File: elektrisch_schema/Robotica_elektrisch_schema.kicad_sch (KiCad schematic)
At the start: 13 parts, among them J1 Raspberry Pi 5, J2 enc1, J3 enc2, J4 H-Brug connector, M1 Motor_DC LINKS, M2 Motor_DC RECHTS, U1 L298N, U2 7.4V -> 6V

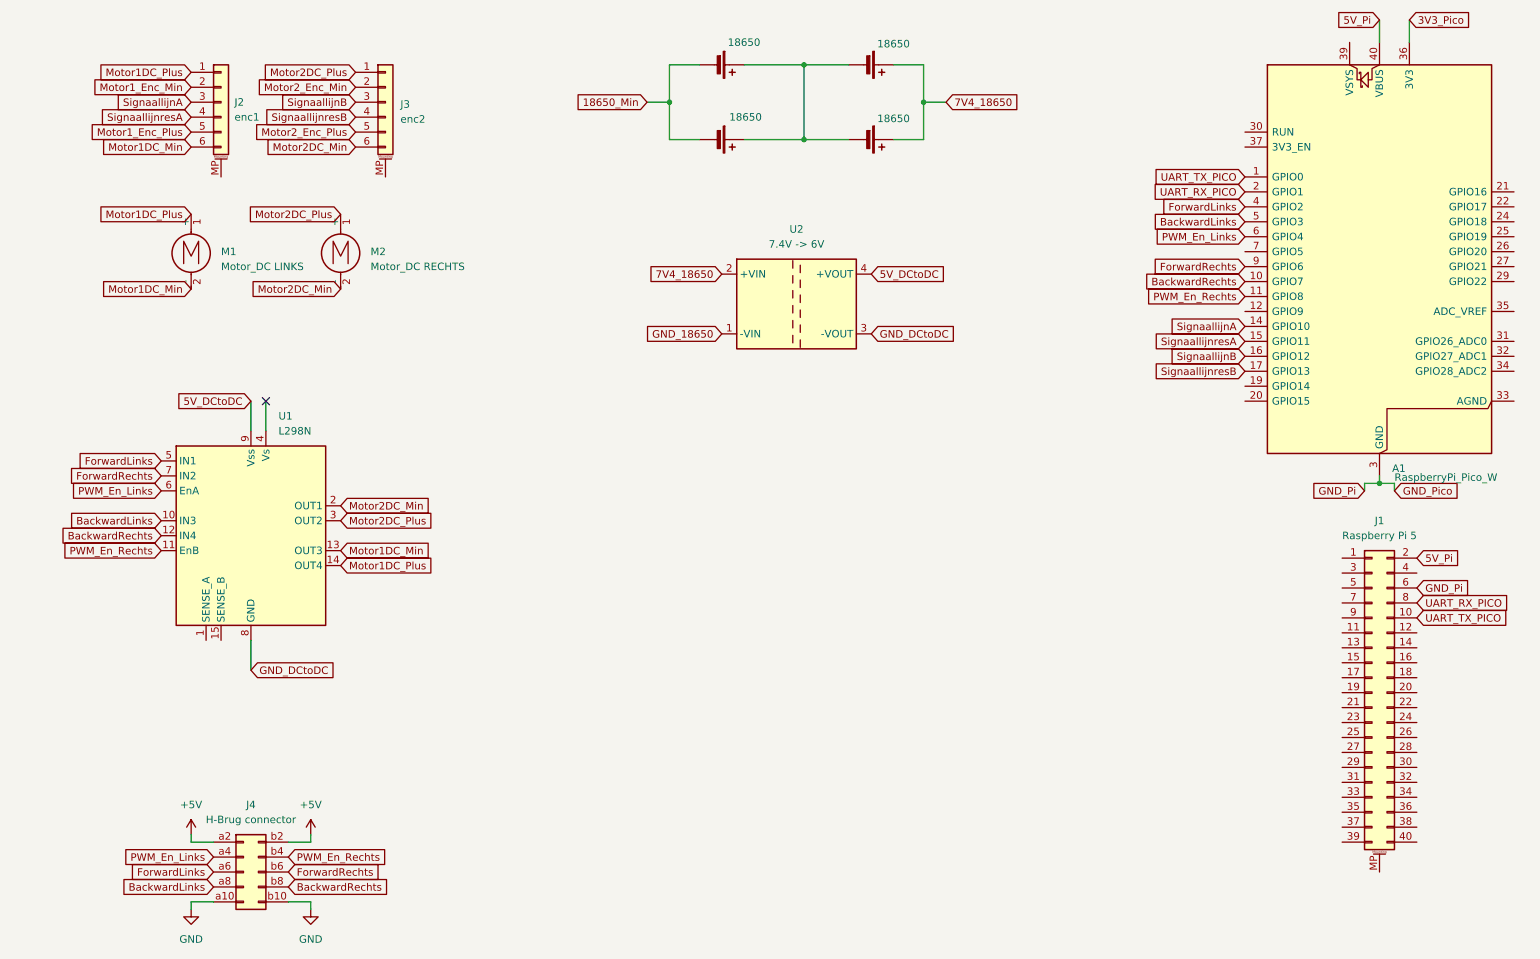
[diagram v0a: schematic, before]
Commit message: Added BNO055 + fixed motor pins
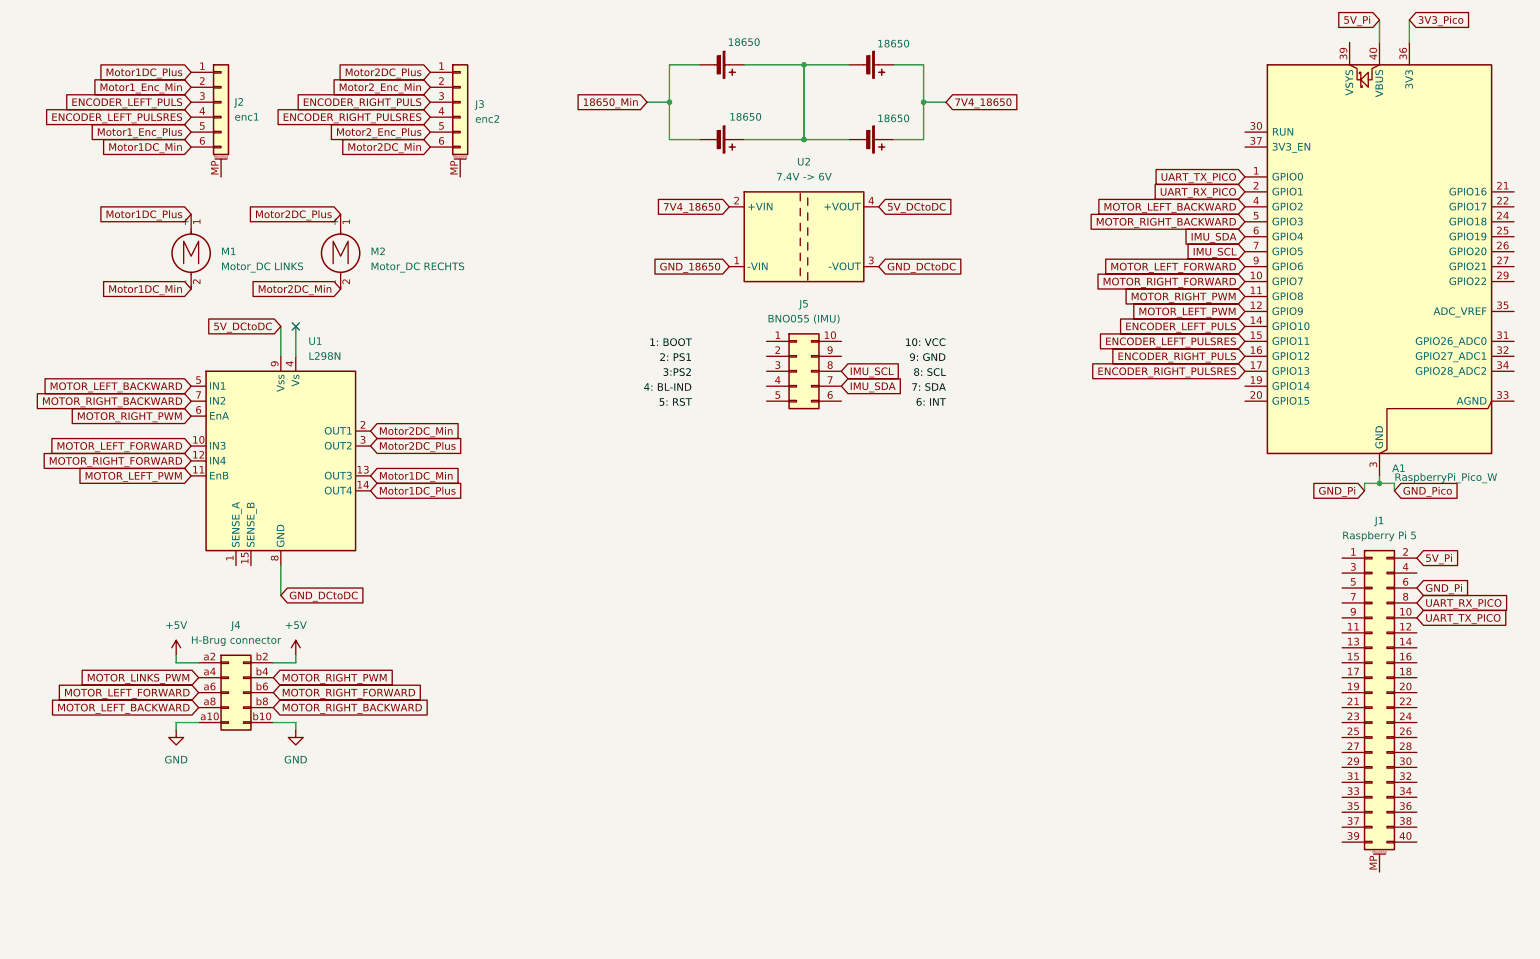
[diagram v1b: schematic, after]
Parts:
- added J5: BNO055 (IMU), symbol Connector_Generic:Conn_02x05_Counter_Clockwise
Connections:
- net MOTOR_LEFT_PWM: now reaches A1.12 (GPIO9)
- net MOTOR_LEFT_PWM: now also U1.11 (EnB)
- net IMU_SCL: now reaches A1.7 (GPIO5)
- net IMU_SCL: now also J5.8 (Pin_8)
- removed net BackwardLinks: A1.5 (GPIO3), J4.a8 (Pin_a8), U1.10 (IN3)
- net BackwardRechts renamed MOTOR_RIGHT_FORWARD
- net MOTOR_RIGHT_FORWARD: now also J4.b6 (Pin_b6); no longer J4.b8 (Pin_b8)
- net ForwardLinks renamed MOTOR_LEFT_BACKWARD
- net MOTOR_LEFT_BACKWARD: now also J4.a8 (Pin_a8); no longer J4.a6 (Pin_a6)
- removed net ForwardRechts: A1.9 (GPIO6), J4.b6 (Pin_b6), U1.7 (IN2)
- removed net PWM_En_Links: A1.6 (GPIO4), J4.a4 (Pin_a4), U1.6 (EnA)
- net PWM_En_Rechts renamed MOTOR_RIGHT_PWM
- net MOTOR_RIGHT_PWM: now also U1.6 (EnA); no longer U1.11 (EnB)
- net SignaallijnA renamed ENCODER_LEFT_PULS
- net SignaallijnB renamed ENCODER_RIGHT_PULS
- net SignaallijnresA renamed ENCODER_LEFT_PULSRES
- net SignaallijnresB renamed ENCODER_RIGHT_PULSRES
- new net IMU_SDA: A1.6 (GPIO4), J5.7 (Pin_7)
- new net MOTOR_LEFT_FORWARD: A1.9 (GPIO6), J4.a6 (Pin_a6), U1.10 (IN3)
- new net MOTOR_LINKS_PWM: J4.a4 (Pin_a4)
- new net MOTOR_RIGHT_BACKWARD: A1.5 (GPIO3), J4.b8 (Pin_b8), U1.7 (IN2)
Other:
- moved on the sheet: J3, J4, U1, U2
